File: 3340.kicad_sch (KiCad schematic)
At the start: 178 parts, among them J1 Conn_01x17, J10 FM1, J11 Conn_01x17, J12 V/OCT2, J13 PULSE2, J14 SAW2, J15 TRI2, J16 SINE2, J17 SYNC2, J18 Conn_01x17, J19 PWM2, J2 Conn_01x17, J20 FM2, J3 V/OCT1, J4 PULSE1, J5 SAW1, J6 TRI1, J7 SINE1, J8 SYNC1, J9 PWM1, Q1 2N3904, Q2 2N3906, Q3 2N3904, Q4 2N3906, Q5 2N3904, Q6 2N3904, SW2 DPDT_OOO, SW3 SW_SPST, U1 TL072, U2 TL074, U3 CEM3340, U4 TL072, U5 CEM3340, U6 TL074

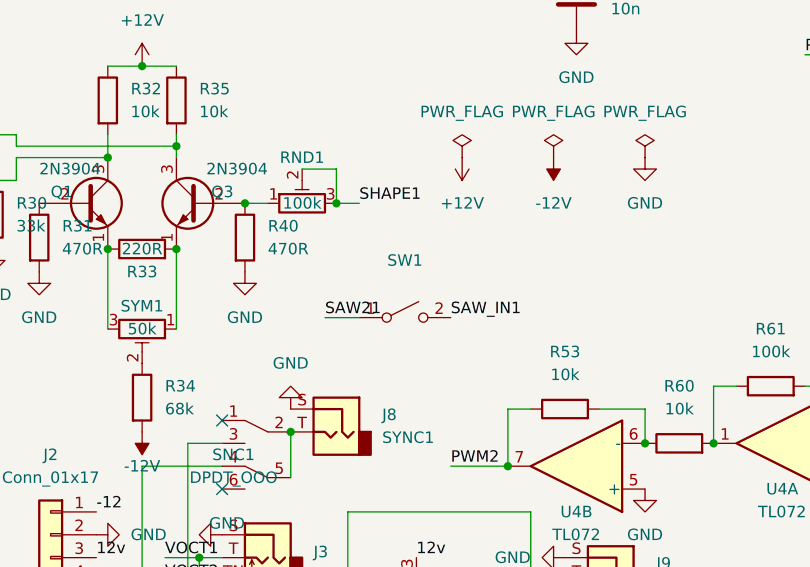
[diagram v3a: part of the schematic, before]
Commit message: Update footprints
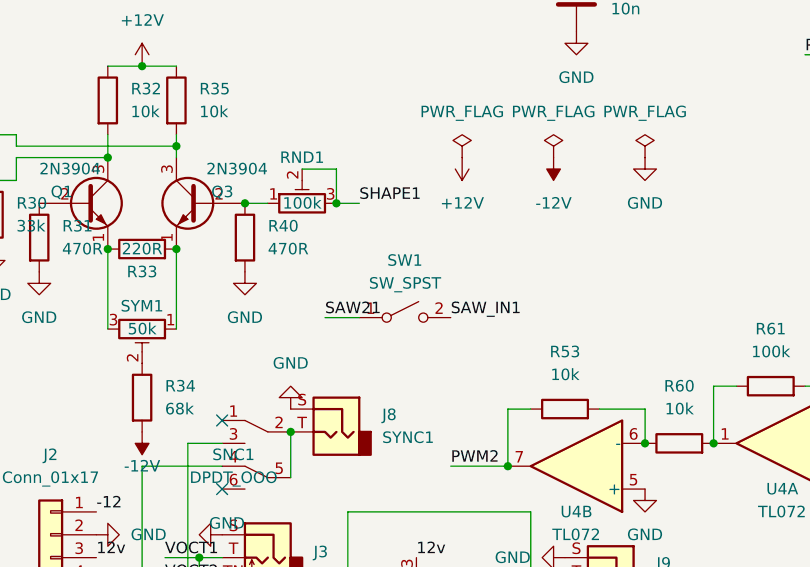
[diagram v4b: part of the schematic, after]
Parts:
- SW1: value (none) -> SW_SPST; footprint (none) -> Button_Switch_THT:SW_SPST_Toggle_Subminiature
- SW3: footprint (none) -> Button_Switch_THT:SW_SPST_Toggle_Subminiature
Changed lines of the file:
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@@
     (pin "2")
     (pin "3")
-    (pin "5")
-    (pin "6")
-    (pin "7")
-    (pin "4")
-    (pin "8")
   )
   (symbol (lib_id "Device:R") (at 92.71 121.92 0) (unit 1)
@@
       (effects (font (size 1.27 1.27)) hide)
     )
-    (pin "1")
-    (pin "2")
-    (pin "3")
-    (pin "5")
-    (pin "6")
-    (pin "7")
     (pin "4")
     (pin "8")
@@
       (effects (font (size 1.27 1.27)) hide)
     )
-    (pin "1")
-    (pin "2")
-    (pin "3")
     (pin "5")
     (pin "6")
     (pin "7")
-    (pin "4")
-    (pin "8")
   )
   (symbol (lib_id "Device:R") (at 78.74 105.41 90) (unit 1)
@@
       (effects (font (size 1.27 1.27)) hide)
     )
-    (pin "1")
-    (pin "2")
-    (pin "3")
-    (pin "5")
-    (pin "6")
-    (pin "7")
     (pin "10")
     (pin "8")
     (pin "9")
-    (pin "12")
-    (pin "13")
-    (pin "14")
-    (pin "11")
-    (pin "4")
   )
   (symbol (lib_id "Device:R") (at 146.05 78.74 90) (unit 1)
@@
       (effects (font (size 1.27 1.27)) hide)
     )
-    (pin "1")
-    (pin "2")
-    (pin "3")
     (pin "5")
     (pin "6")
     (pin "7")
-    (pin "10")
-    (pin "8")
-    (pin "9")
-    (pin "12")
-    (pin "13")
-    (pin "14")
-    (pin "11")
-    (pin "4")
   )
   (symbol (lib_id "Device:C_Polarized") (at 60.96 151.13 0) (unit 1)
@@
     (in_bom yes) (on_board yes) (fields_autoplaced)
     (property "Reference" "SW1" (id 0) (at 133.35 124.46 0))
-    (property "Value" "" (id 1) (at 133.35 127 0))
-    (property "Footprint" "" (id 2) (at 133.35 130.81 0)
+    (property "Value" "SW_SPST" (id 1) (at 133.35 127 0))
+    (property "Footprint" "Button_Switch_THT:SW_SPST_Toggle_Subminiature" (id 2) (at 133.35 130.81 0)
       (effects (font (size 1.27 1.27)) hide)
     )
@@
       (effects (font (size 1.27 1.27)) hide)
     )
-    (pin "1")
-    (pin "2")
-    (pin "3")
-    (pin "5")
-    (pin "6")
-    (pin "7")
     (pin "4")
     (pin "8")
@@
     (pin "2")
     (pin "3")
-    (pin "5")
-    (pin "6")
-    (pin "7")
-    (pin "10")
-    (pin "8")
-    (pin "9")
-    (pin "12")
-    (pin "13")
-    (pin "14")
-    (pin "11")
-    (pin "4")
   )
   (symbol (lib_id "power:GND") (at 160.02 149.86 0) (unit 1)
@@
     (pin "2")
     (pin "3")
-    (pin "5")
-    (pin "6")
-    (pin "7")
-    (pin "4")
-    (pin "8")
   )
   (symbol (lib_id "power:-12V") (at 78.74 134.62 270) (unit 1)
@@
     (property "Reference" "SW3" (id 0) (at 270.51 27.94 0))
     (property "Value" "SW_SPST" (id 1) (at 270.51 30.48 0))
-    (property "Footprint" "" (id 2) (at 270.51 34.29 0)
+    (property "Footprint" "Button_Switch_THT:SW_SPST_Toggle_Subminiature" (id 2) (at 270.51 34.29 0)
       (effects (font (size 1.27 1.27)) hide)
     )
@@
       (effects (font (size 1.27 1.27)) hide)
     )
-    (pin "1")
-    (pin "2")
-    (pin "3")
-    (pin "5")
-    (pin "6")
-    (pin "7")
-    (pin "10")
-    (pin "8")
-    (pin "9")
-    (pin "12")
-    (pin "13")
-    (pin "14")
     (pin "11")
     (pin "4")
@@
       (effects (font (size 1.27 1.27)) hide)
     )
-    (pin "1")
-    (pin "2")
-    (pin "3")
     (pin "5")
     (pin "6")
     (pin "7")
-    (pin "4")
-    (pin "8")
   )
   (symbol (lib_id "Device:R") (at 25.4 181.61 90) (unit 1)
@@
     (pin "2")
     (pin "3")
-    (pin "5")
-    (pin "6")
-    (pin "7")
-    (pin "10")
-    (pin "8")
-    (pin "9")
-    (pin "12")
-    (pin "13")
-    (pin "14")
-    (pin "11")
-    (pin "4")
   )
   (symbol (lib_id "Device:D") (at 40.64 21.59 0) (mirror y) (unit 1)
@@
       (effects (font (size 1.27 1.27)) hide)
     )
-    (pin "1")
-    (pin "2")
-    (pin "3")
-    (pin "5")
-    (pin "6")
-    (pin "7")
-    (pin "10")
-    (pin "8")
-    (pin "9")
-    (pin "12")
-    (pin "13")
-    (pin "14")
     (pin "11")
     (pin "4")
@@
       (effects (font (size 1.27 1.27)) hide)
     )
-    (pin "1")
-    (pin "2")
-    (pin "3")
-    (pin "5")
-    (pin "6")
-    (pin "7")
-    (pin "10")
-    (pin "8")
-    (pin "9")
     (pin "12")
     (pin "13")
     (pin "14")
-    (pin "11")
-    (pin "4")
   )
   (symbol (lib_id "Connector:AudioJack2") (at 233.68 161.29 0) (mirror y) (unit 1)
@@
       (effects (font (size 1.27 1.27)) hide)
     )
-    (pin "1")
-    (pin "2")
-    (pin "3")
-    (pin "5")
-    (pin "6")
-    (pin "7")
     (pin "10")
     (pin "8")
     (pin "9")
-    (pin "12")
-    (pin "13")
-    (pin "14")
-    (pin "11")
-    (pin "4")
   )
   (symbol (lib_id "Device:R") (at 36.83 17.78 0) (mirror y) (unit 1)
@@
       (effects (font (size 1.27 1.27)) hide)
     )
-    (pin "1")
-    (pin "2")
-    (pin "3")
-    (pin "5")
-    (pin "6")
-    (pin "7")
-    (pin "10")
-    (pin "8")
-    (pin "9")
     (pin "12")
     (pin "13")
     (pin "14")
-    (pin "11")
-    (pin "4")
   )
   (symbol (lib_id "power:+12V") (at 26.67 170.18 270) (unit 1)
@@
       (effects (font (size 1.27 1.27)) hide)
     )
-    (pin "1")
-    (pin "2")
-    (pin "3")
     (pin "5")
     (pin "6")
     (pin "7")
-    (pin "10")
-    (pin "8")
-    (pin "9")
-    (pin "12")
-    (pin "13")
-    (pin "14")
-    (pin "11")
-    (pin "4")
   )
   (symbol (lib_id "Device:R") (at 67.31 77.47 0) (unit 1)
@@
     )
     (path "/4f77388d-b9d0-4512-8c08-99b0c79a19a3"
-      (reference "SW1") (unit 1) (value "SW_SPST") (footprint "")
+      (reference "SW1") (unit 1) (value "SW_SPST") (footprint "Button_Switch_THT:SW_SPST_Toggle_Subminiature")
     )
     (path "/ca8492c6-a762-403e-a1f8-477330a423ed"
@@
     )
     (path "/8e0d0ff3-73a6-4f79-ba76-e56792c0dc09"
-      (reference "SW3") (unit 1) (value "SW_SPST") (footprint "")
+      (reference "SW3") (unit 1) (value "SW_SPST") (footprint "Button_Switch_THT:SW_SPST_Toggle_Subminiature")
     )
     (path "/54012768-bb14-48fe-ad71-d0399b5b51ab"

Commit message: Mark switch holes
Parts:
- COARSE1, COARSE2, FINE1, FINE2, PW1, PW2, PWM1, PWM2: footprint Potentiometer_THT:Potentiometer_Alpha_RD901F-40-00D_Single_Vertical -> Potentiometer_THT:Potentiometer_Alpha_RD901F-40-00D_Single_Vertical_CircularHoles
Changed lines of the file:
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@@
       (effects (font (size 1.27 1.27)) (justify right))
     )
-    (property "Footprint" "Potentiometer_THT:Potentiometer_Alpha_RD901F-40-00D_Single_Vertical" (id 2) (at 134.62 184.15 0)
+    (property "Footprint" "Potentiometer_THT:Potentiometer_Alpha_RD901F-40-00D_Single_Vertical_CircularHoles" (id 2) (at 134.62 184.15 0)
       (effects (font (size 1.27 1.27)) hide)
     )
@@
       (effects (font (size 1.27 1.27)) (justify right))
     )
-    (property "Footprint" "Potentiometer_THT:Potentiometer_Alpha_RD901F-40-00D_Single_Vertical" (id 2) (at 266.7 134.62 0)
+    (property "Footprint" "Potentiometer_THT:Potentiometer_Alpha_RD901F-40-00D_Single_Vertical_CircularHoles" (id 2) (at 266.7 134.62 0)
       (effects (font (size 1.27 1.27)) hide)
     )
@@
       (effects (font (size 1.27 1.27)) (justify right))
     )
-    (property "Footprint" "Potentiometer_THT:Potentiometer_Alpha_RD901F-40-00D_Single_Vertical" (id 2) (at 151.13 163.83 0)
+    (property "Footprint" "Potentiometer_THT:Potentiometer_Alpha_RD901F-40-00D_Single_Vertical_CircularHoles" (id 2) (at 151.13 163.83 0)
       (effects (font (size 1.27 1.27)) hide)
     )
@@
       (effects (font (size 1.27 1.27)) (justify right))
     )
-    (property "Footprint" "Potentiometer_THT:Potentiometer_Alpha_RD901F-40-00D_Single_Vertical" (id 2) (at 250.19 154.94 0)
+    (property "Footprint" "Potentiometer_THT:Potentiometer_Alpha_RD901F-40-00D_Single_Vertical_CircularHoles" (id 2) (at 250.19 154.94 0)
       (effects (font (size 1.27 1.27)) hide)
     )
@@
       (effects (font (size 1.27 1.27)) (justify right))
     )
-    (property "Footprint" "Potentiometer_THT:Potentiometer_Alpha_RD901F-40-00D_Single_Vertical" (id 2) (at 134.62 172.72 0)
+    (property "Footprint" "Potentiometer_THT:Potentiometer_Alpha_RD901F-40-00D_Single_Vertical_CircularHoles" (id 2) (at 134.62 172.72 0)
       (effects (font (size 1.27 1.27)) hide)
     )
@@
       (effects (font (size 1.27 1.27)) (justify right))
     )
-    (property "Footprint" "Potentiometer_THT:Potentiometer_Alpha_RD901F-40-00D_Single_Vertical" (id 2) (at 250.19 132.08 0)
+    (property "Footprint" "Potentiometer_THT:Potentiometer_Alpha_RD901F-40-00D_Single_Vertical_CircularHoles" (id 2) (at 250.19 132.08 0)
       (effects (font (size 1.27 1.27)) hide)
     )
@@
       (effects (font (size 1.27 1.27)) (justify right))
     )
-    (property "Footprint" "Potentiometer_THT:Potentiometer_Alpha_RD901F-40-00D_Single_Vertical" (id 2) (at 250.19 143.51 0)
+    (property "Footprint" "Potentiometer_THT:Potentiometer_Alpha_RD901F-40-00D_Single_Vertical_CircularHoles" (id 2) (at 250.19 143.51 0)
       (effects (font (size 1.27 1.27)) hide)
     )
@@
       (effects (font (size 1.27 1.27)) (justify right))
     )
-    (property "Footprint" "Potentiometer_THT:Potentiometer_Alpha_RD901F-40-00D_Single_Vertical" (id 2) (at 134.62 161.29 0)
+    (property "Footprint" "Potentiometer_THT:Potentiometer_Alpha_RD901F-40-00D_Single_Vertical_CircularHoles" (id 2) (at 134.62 161.29 0)
       (effects (font (size 1.27 1.27)) hide)
     )
@@
     )
     (path "/e9cea4d7-c35e-498b-956b-e9112d74ca4d"
-      (reference "COARSE1") (unit 1) (value "B20k") (footprint "Potentiometer_THT:Potentiometer_Alpha_RD901F-40-00D_Single_Vertical")
+      (reference "COARSE1") (unit 1) (value "B20k") (footprint "Potentiometer_THT:Potentiometer_Alpha_RD901F-40-00D_Single_Vertical_CircularHoles")
     )
     (path "/9277be02-0ca4-43e5-a1b7-432d125d1d18"
-      (reference "COARSE2") (unit 1) (value "B20k") (footprint "Potentiometer_THT:Potentiometer_Alpha_RD901F-40-00D_Single_Vertical")
+      (reference "COARSE2") (unit 1) (value "B20k") (footprint "Potentiometer_THT:Potentiometer_Alpha_RD901F-40-00D_Single_Vertical_CircularHoles")
     )
     (path "/b2ccb769-0cb0-4378-9666-0b43931cfcd4"
@@
     )
     (path "/80dece0f-79cb-4af2-b46d-a98bdd4ae117"
-      (reference "FINE1") (unit 1) (value "B20k") (footprint "Potentiometer_THT:Potentiometer_Alpha_RD901F-40-00D_Single_Vertical")
+      (reference "FINE1") (unit 1) (value "B20k") (footprint "Potentiometer_THT:Potentiometer_Alpha_RD901F-40-00D_Single_Vertical_CircularHoles")
     )
     (path "/dd257896-399c-4505-afdc-34465a87c5b8"
-      (reference "FINE2") (unit 1) (value "B20k") (footprint "Potentiometer_THT:Potentiometer_Alpha_RD901F-40-00D_Single_Vertical")
+      (reference "FINE2") (unit 1) (value "B20k") (footprint "Potentiometer_THT:Potentiometer_Alpha_RD901F-40-00D_Single_Vertical_CircularHoles")
     )
     (path "/d2def891-76d1-4589-af17-41697317b168"
@@
     )
     (path "/3e6b0dbb-33b8-493d-a136-d7bd55d73615"
-      (reference "PW1") (unit 1) (value "B100k") (footprint "Potentiometer_THT:Potentiometer_Alpha_RD901F-40-00D_Single_Vertical")
+      (reference "PW1") (unit 1) (value "B100k") (footprint "Potentiometer_THT:Potentiometer_Alpha_RD901F-40-00D_Single_Vertical_CircularHoles")
     )
     (path "/75911324-a685-49e9-9390-e212534f5029"
-      (reference "PW2") (unit 1) (value "B100k") (footprint "Potentiometer_THT:Potentiometer_Alpha_RD901F-40-00D_Single_Vertical")
+      (reference "PW2") (unit 1) (value "B100k") (footprint "Potentiometer_THT:Potentiometer_Alpha_RD901F-40-00D_Single_Vertical_CircularHoles")
     )
     (path "/48f1df72-21f5-44e6-8e10-0c601f8cf333"
-      (reference "PWM1") (unit 1) (value "B100k") (footprint "Potentiometer_THT:Potentiometer_Alpha_RD901F-40-00D_Single_Vertical")
+      (reference "PWM1") (unit 1) (value "B100k") (footprint "Potentiometer_THT:Potentiometer_Alpha_RD901F-40-00D_Single_Vertical_CircularHoles")
     )
     (path "/4598e6e2-f73c-4cf5-ac6e-9af0bf61ba76"
-      (reference "PWM2") (unit 1) (value "B100k") (footprint "Potentiometer_THT:Potentiometer_Alpha_RD901F-40-00D_Single_Vertical")
+      (reference "PWM2") (unit 1) (value "B100k") (footprint "Potentiometer_THT:Potentiometer_Alpha_RD901F-40-00D_Single_Vertical_CircularHoles")
     )
     (path "/e27c3ebf-ece4-4dd3-a647-c521203a951a"
